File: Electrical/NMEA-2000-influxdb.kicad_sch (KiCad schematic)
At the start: 13 parts, among them J1 Conn_01x04, J2 Conn_01x04, J3 Conn_02x04, U1 LM7805_TO220, U2 ESP32_NODEMCU, U3 RTC-Module, U4 SD-Card-Module, U5 SN65HVD230

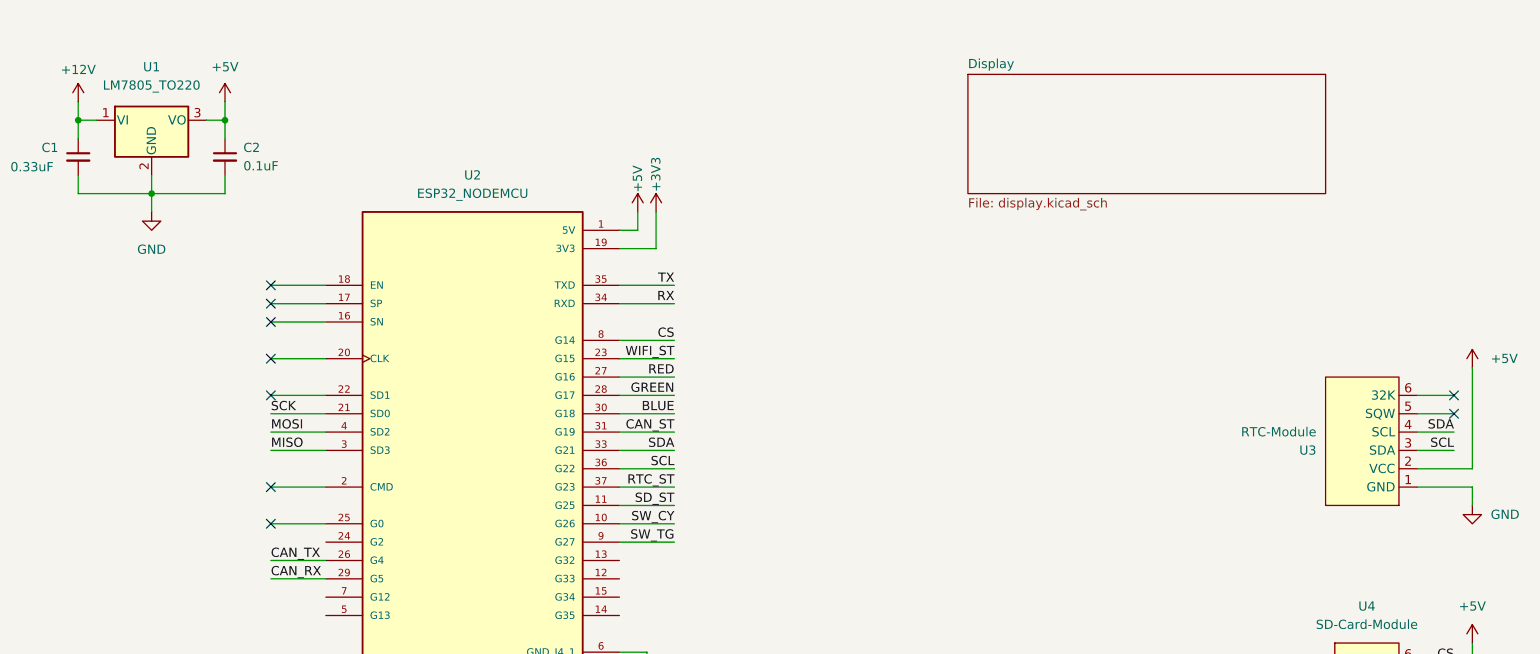
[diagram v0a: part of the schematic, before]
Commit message: Removed RTC-Module
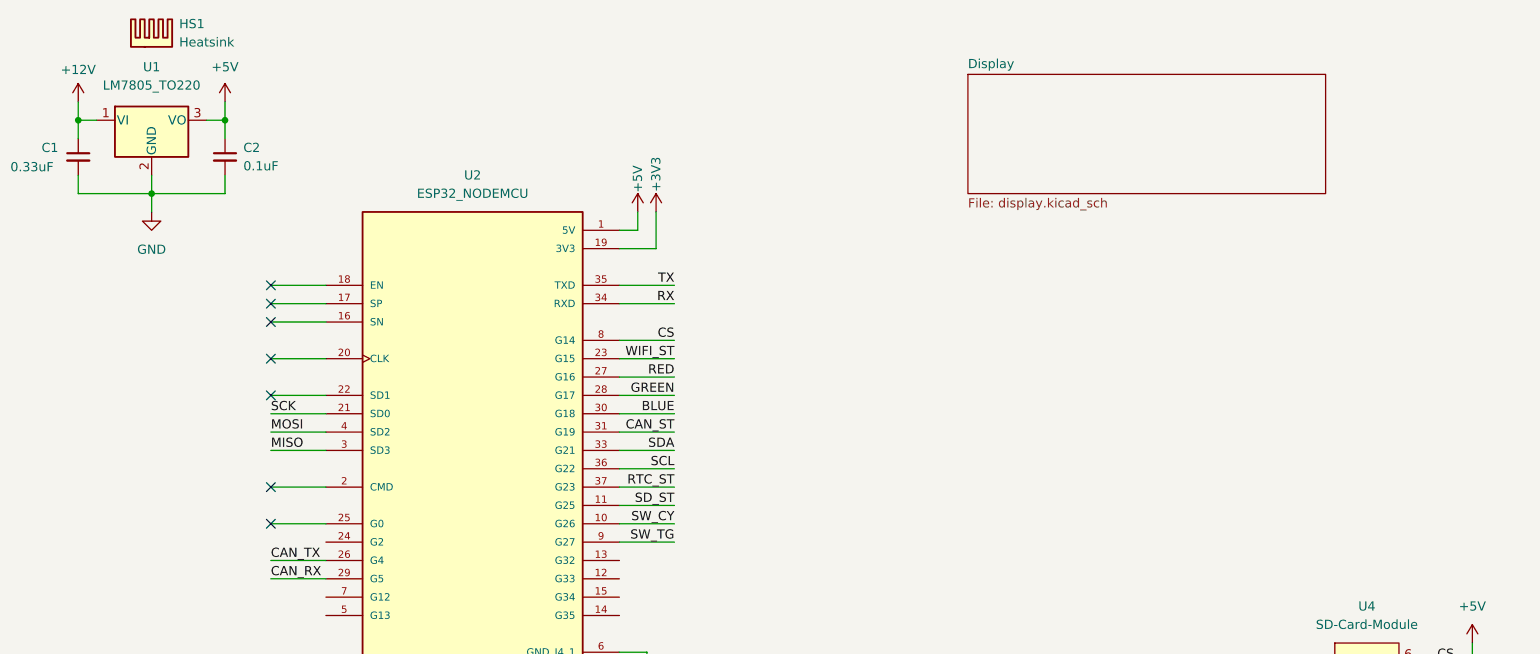
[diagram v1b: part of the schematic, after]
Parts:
- removed U3: RTC-Module, Connector_PinSocket_2.54mm:PinSocket_1x06_P2.54mm_Horizontal, symbol RTC-Module:RTC-Module
- added HS1: Heatsink, symbol Mechanical:Heatsink
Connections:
- no-connect marks 10 -> 8

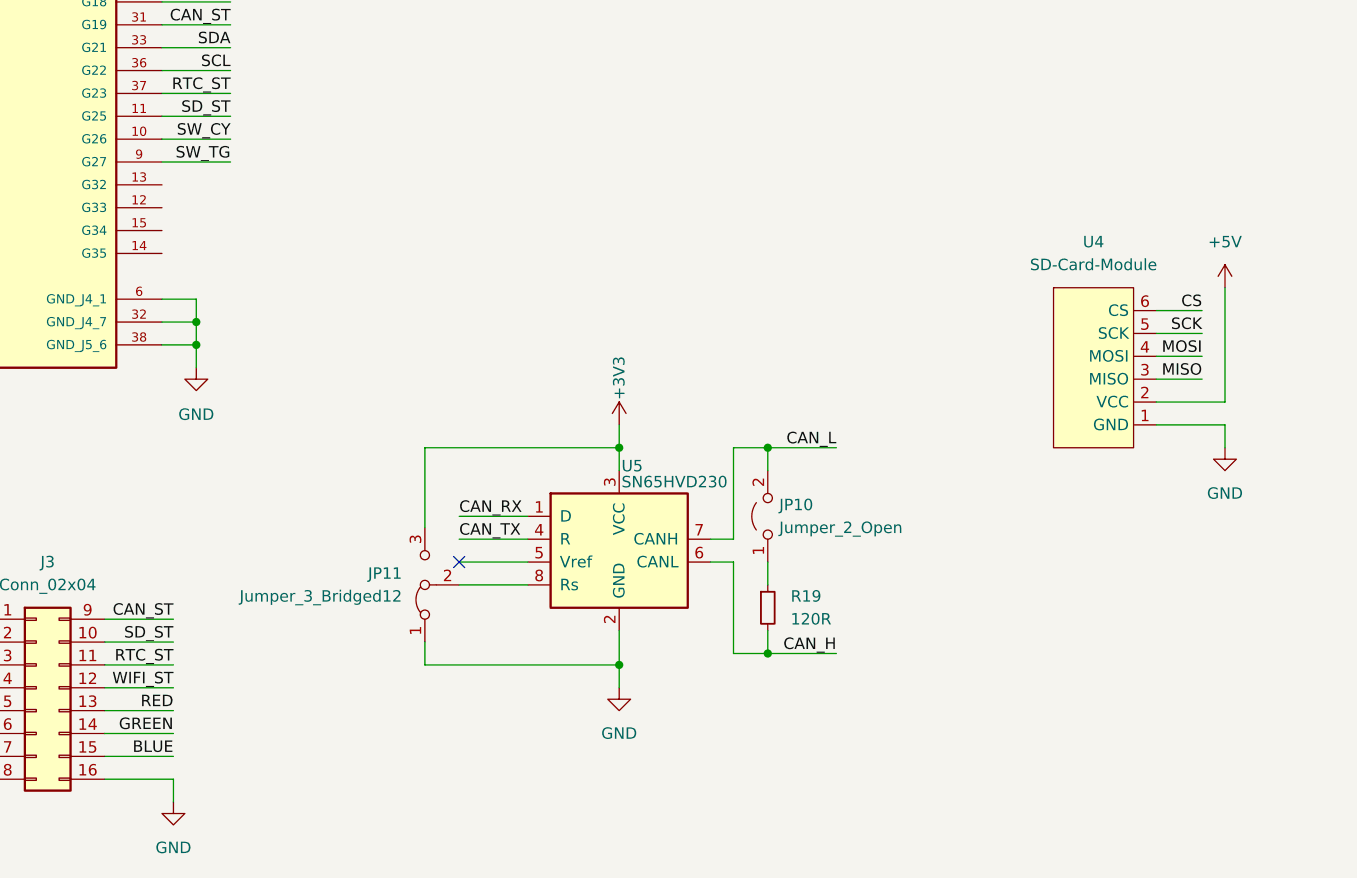
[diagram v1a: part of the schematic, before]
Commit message: Added Backup CAN Transceiver Module Switched Push Button for SPST Switch Added Heatsink for LM7805
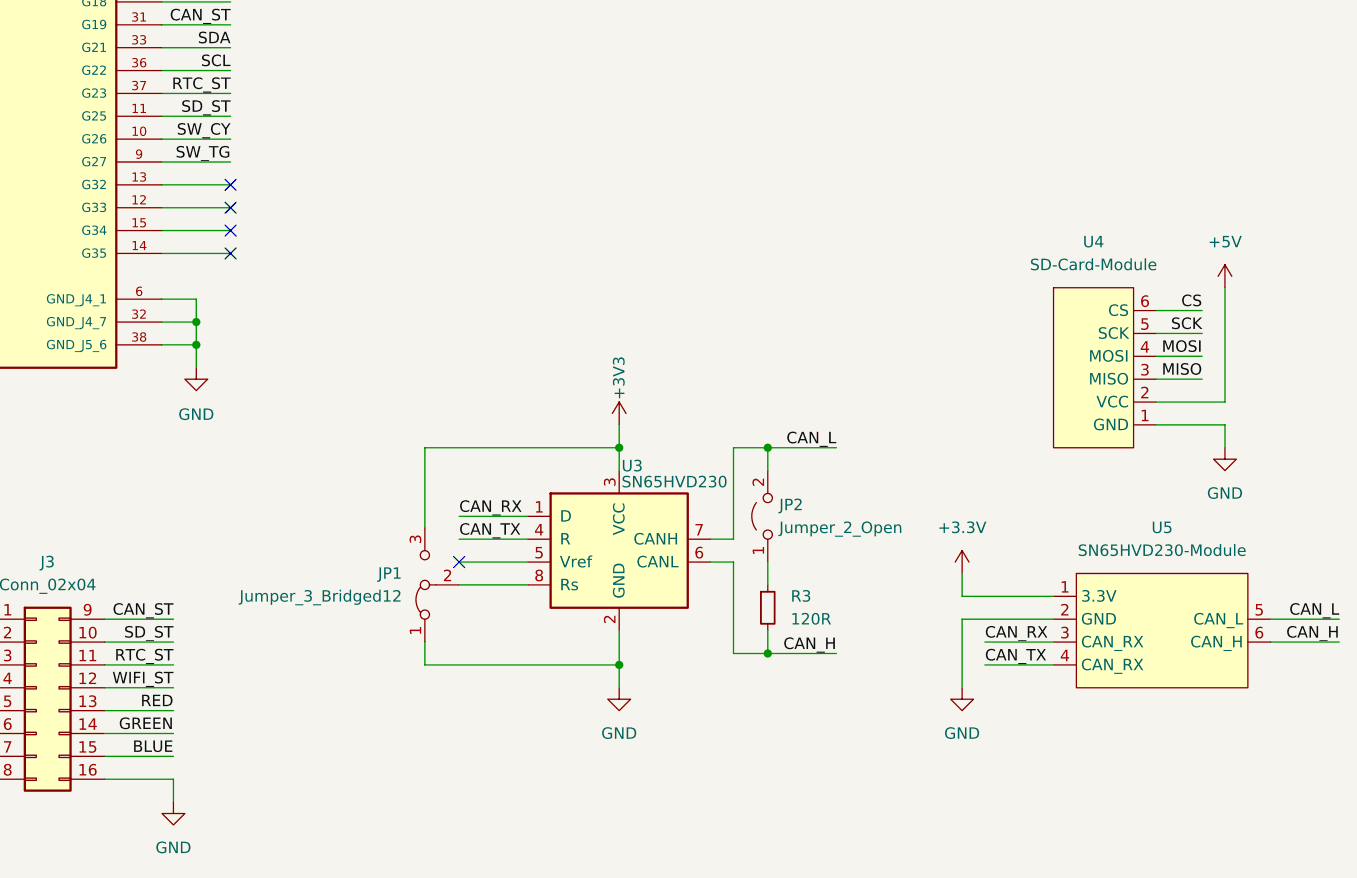
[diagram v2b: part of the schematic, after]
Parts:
- added U5: SN65HVD230-Module, Connector_PinSocket_2.54mm:PinSocket_1x04_P2.54mm_Horizontal, symbol sn65hvd230-module:SN65HVD230-Module
- renumbered JP11 to JP1, JP10 to JP2, R19 to R3, U5 to U3
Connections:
- net CAN_H: now also U5.6 (CAN_H)
- net CAN_L: now also U5.5 (CAN_L)
- net CAN_RX: now also U5.3 (CAN_RX)
- net CAN_TX: now also U5.4 (CAN_RX)
- net GND: now also U5.2 (GND)
- new net +3.3V: U5.1 (3.3V)
- no-connect marks 8 -> 12

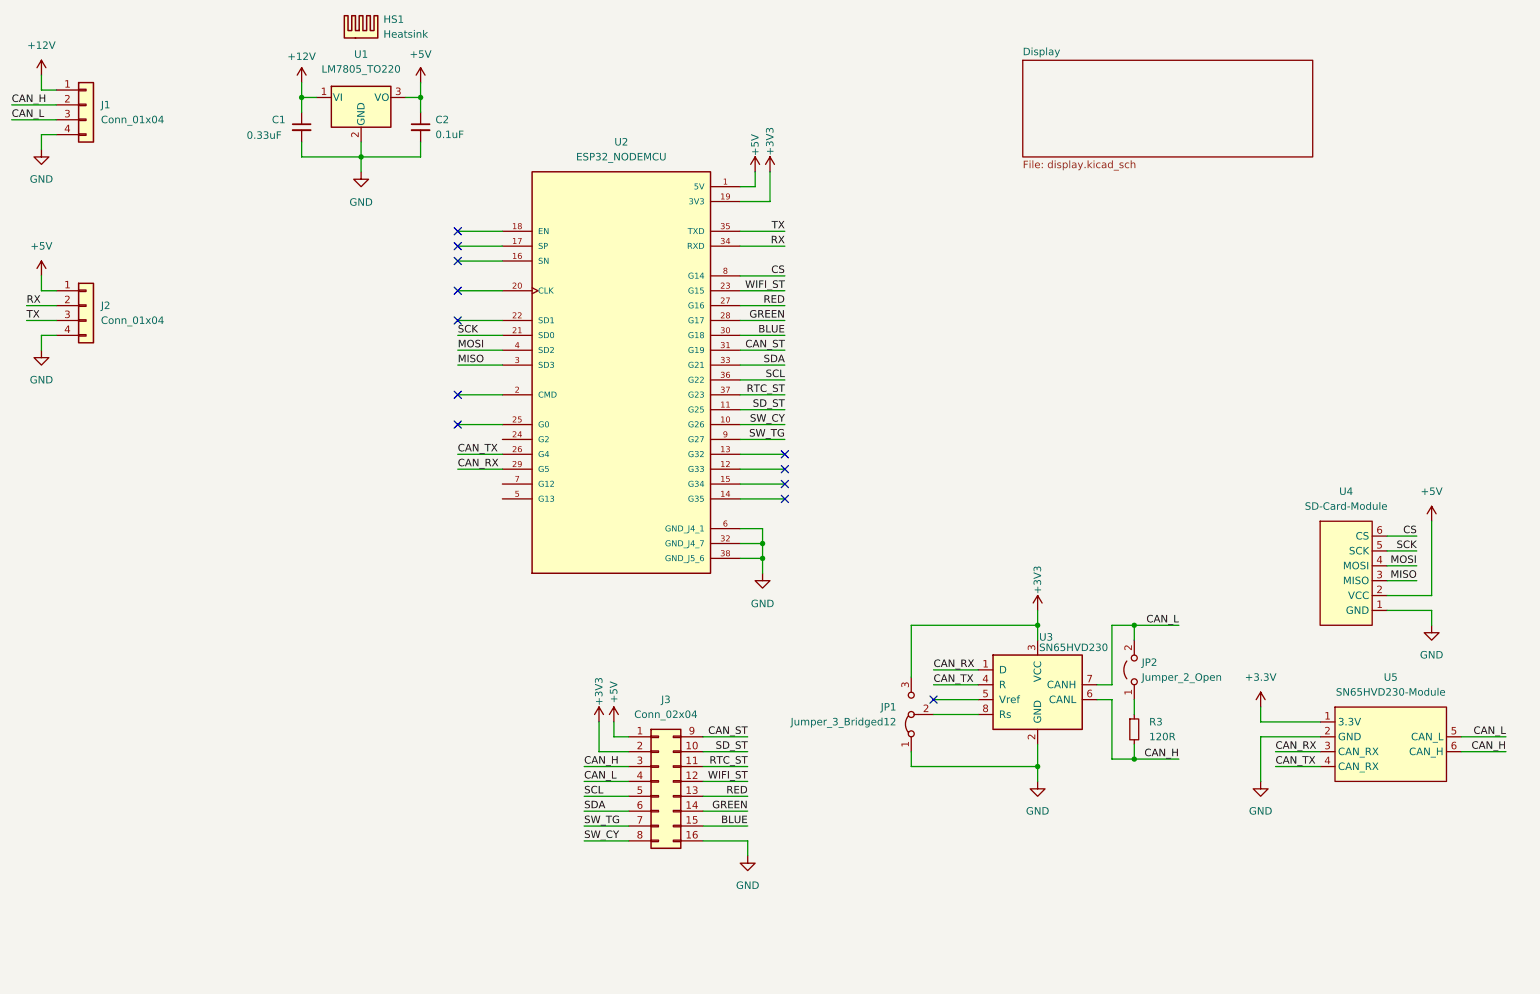
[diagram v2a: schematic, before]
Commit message: Added VMOT Added Power LEDs
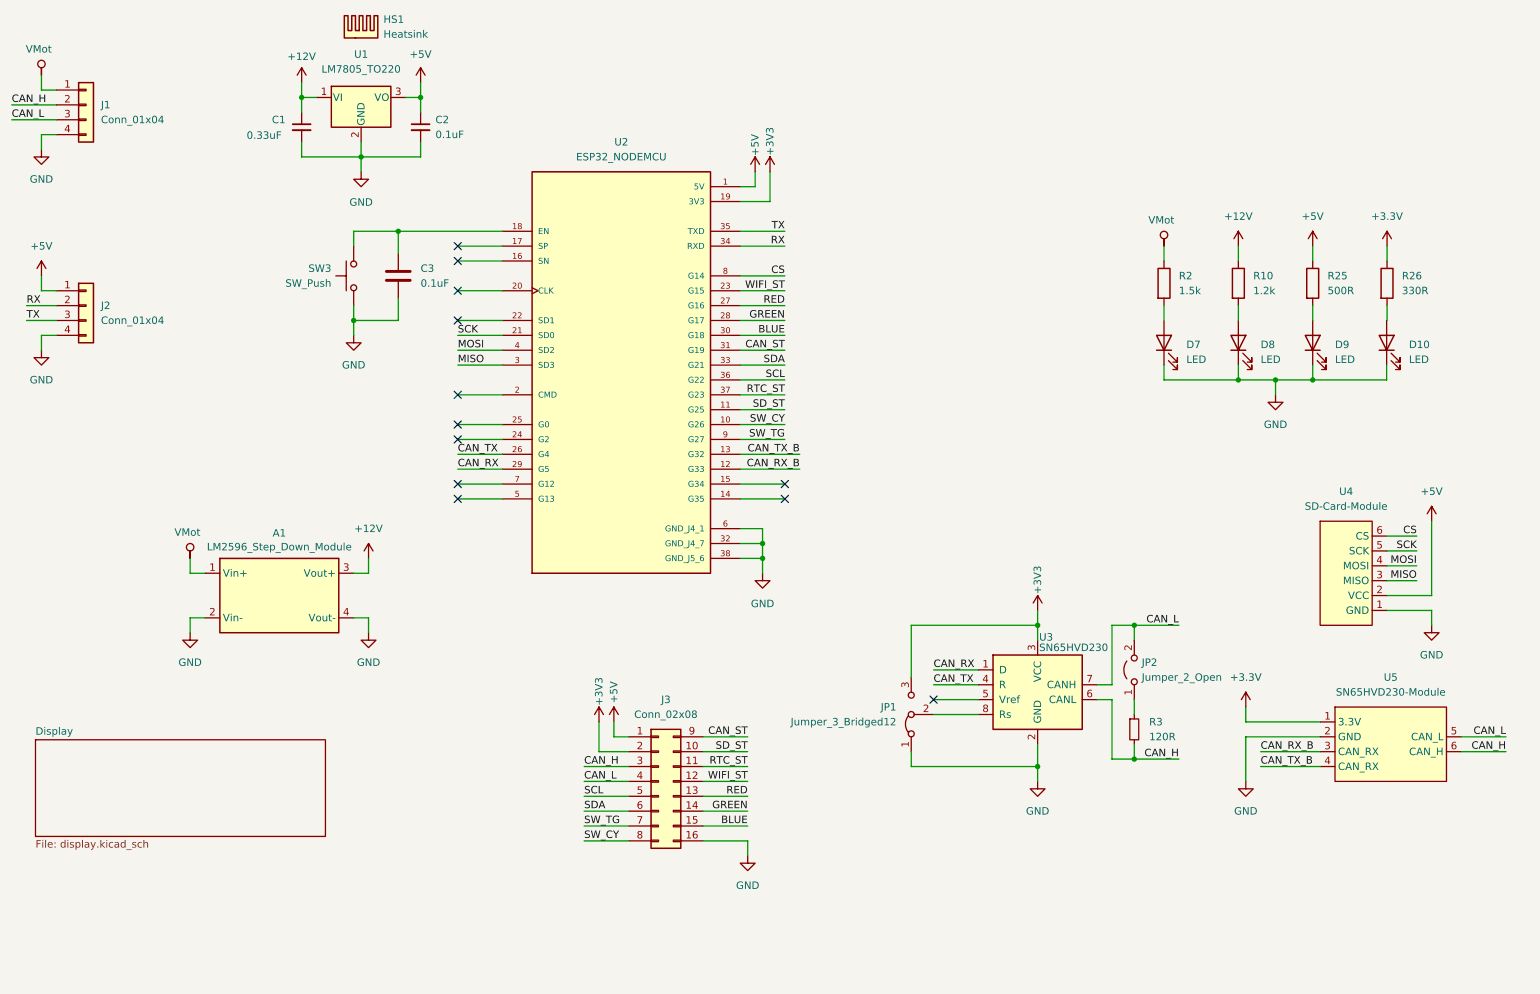
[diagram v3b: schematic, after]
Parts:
- added A1: LM2596_Step_Down_Module, MPCNC_Shield_Footprints:LM2596_Step_Down_Module-21.3x43.6mm, symbol MPCNC_Shield_Symbols:LM2596_Step_Down_Module
- added C3: 0.1uF, symbol Device:C
- added D10, D7, D8, D9: LED, symbol Device:LED
- added R10: 1.2k, symbol Device:R
- added R2: 1.5k, symbol Device:R
- added R25: 500R, symbol Device:R
- added R26: 330R, symbol Device:R
- added SW3: SW_Push, symbol Switch:SW_Push
- J3: value Conn_02x04 -> Conn_02x08
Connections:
- net +12V: now also A1.3 (Vout+), R10.1; no longer J1.1 (Pin_1)
- net +3.3V: now also R26.1
- net +5V: now also R25.1
- net CAN_RX: no longer U5.3 (CAN_RX)
- net CAN_TX: no longer U5.4 (CAN_RX)
- net GND: now also A1.2 (Vin-), A1.4 (Vout-), C3.2, D10.1 (K), D7.1 (K), D8.1 (K), D9.1 (K), SW3.1
- net CAN_RX_B: now reaches U2.12 (G33)
- net CAN_RX_B: now also U5.3 (CAN_RX)
- net CAN_TX_B: now reaches U2.13 (G32)
- net CAN_TX_B: now also U5.4 (CAN_RX)
- net at U2.18 (EN): now also C3.1, SW3.2
- new net: D8.2 (A), R10.2
- new net: D7.2 (A), R2.2
- new net: D9.2 (A), R25.2
- new net VMot: A1.1 (Vin+), J1.1 (Pin_1), R2.1
